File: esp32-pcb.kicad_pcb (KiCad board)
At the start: 2 copper layers, 25.2 x 59.4 mm, 50 parts, among them J1 Conn_01x15_Male, J2 Conn_01x15_Male, Q1 SI2333DDS-T1-GE3, Q2 BSS138Q-7-F, Q3 MMBT3904, Q4 MMBT3904, Q5 BSS138Q-7-F, SW1 RESET, SW2 USER, SW3 SW_DIP_x04, U1 TLV75533, U2 ESP32-WROOM-32, U3 CP2102N-A01-GQFN24

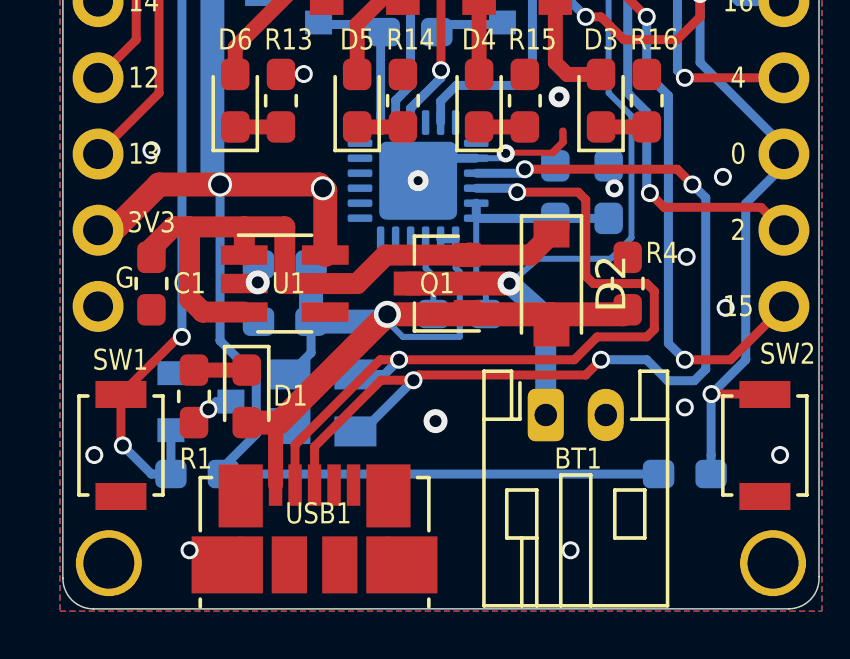
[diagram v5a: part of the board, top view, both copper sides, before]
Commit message: Fix D2 text. Eliminate overlaps
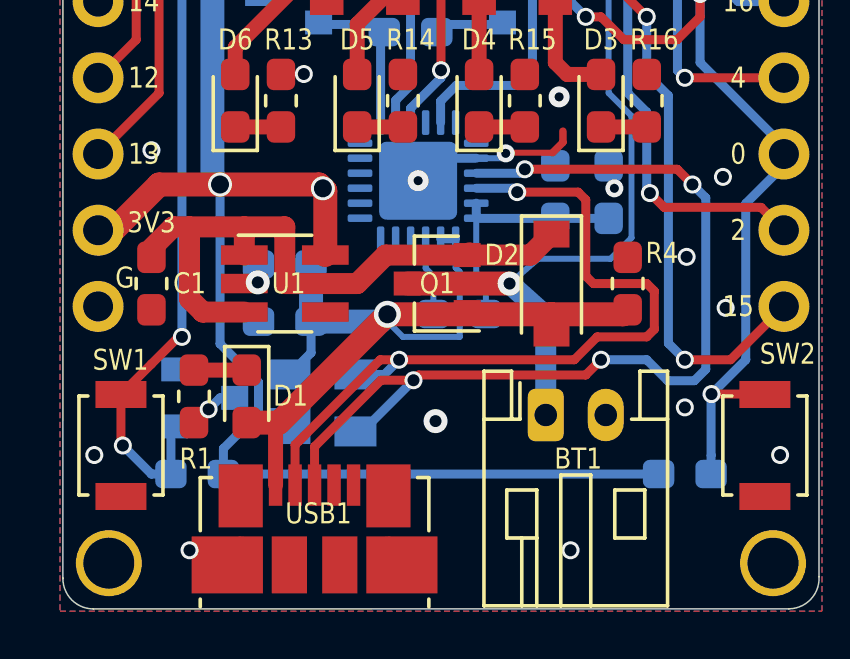
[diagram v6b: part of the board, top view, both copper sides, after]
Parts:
- moved Q5 0.18 mm to (133.9, 120.7)

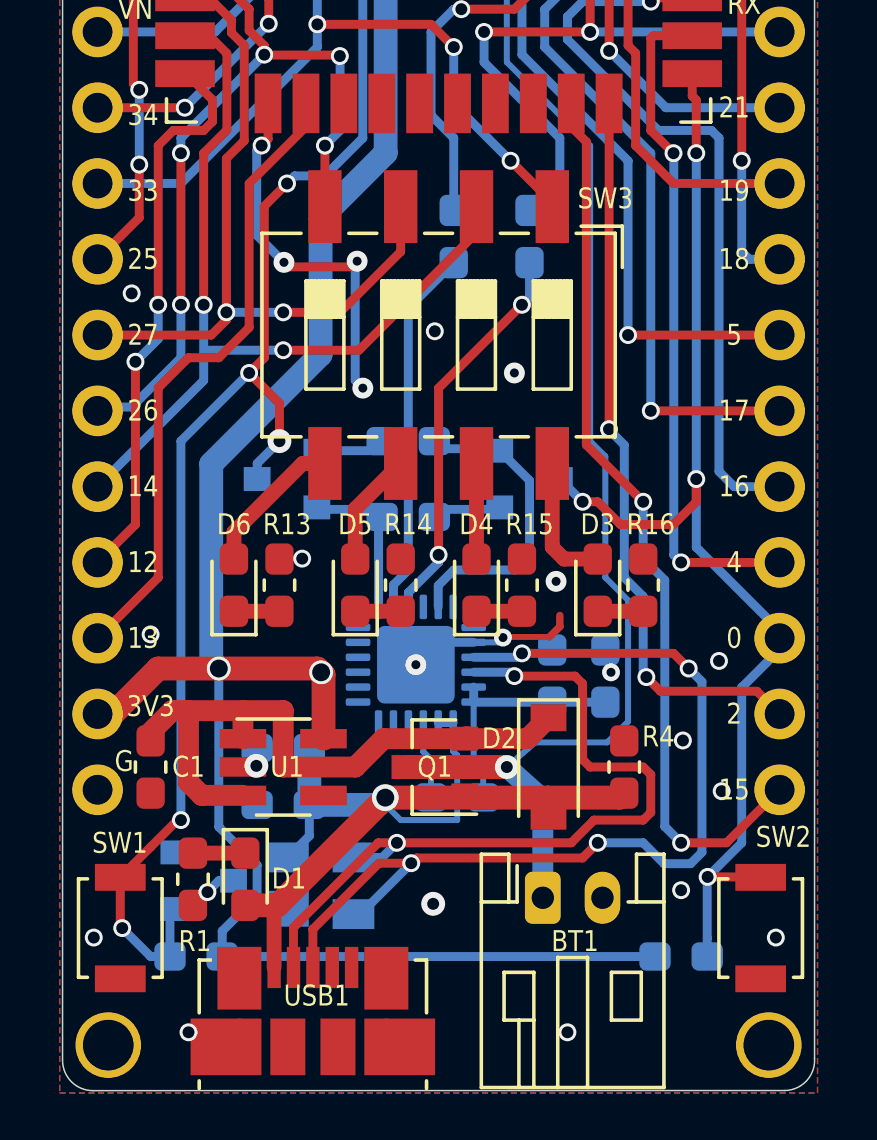
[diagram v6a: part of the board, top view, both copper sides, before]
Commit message: Connect D4 to IO12
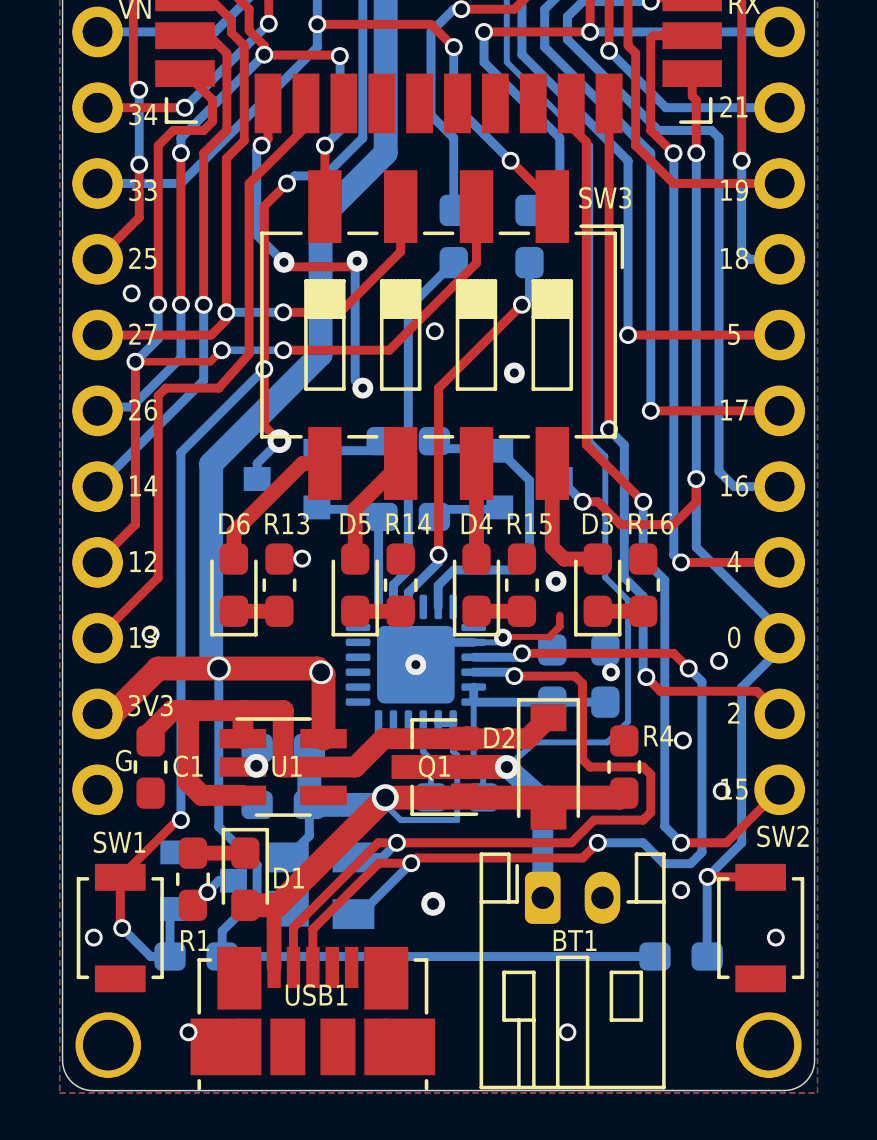
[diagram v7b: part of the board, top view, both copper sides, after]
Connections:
- SW3 pad 2: ESP_IO14 -> ESP_IO12
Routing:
- net ESP_IO12: track 19.0 -> 34.5 mm, vias 2 -> 4
- net ESP_IO14: track 30.2 -> 18.7 mm, vias 2 -> 1

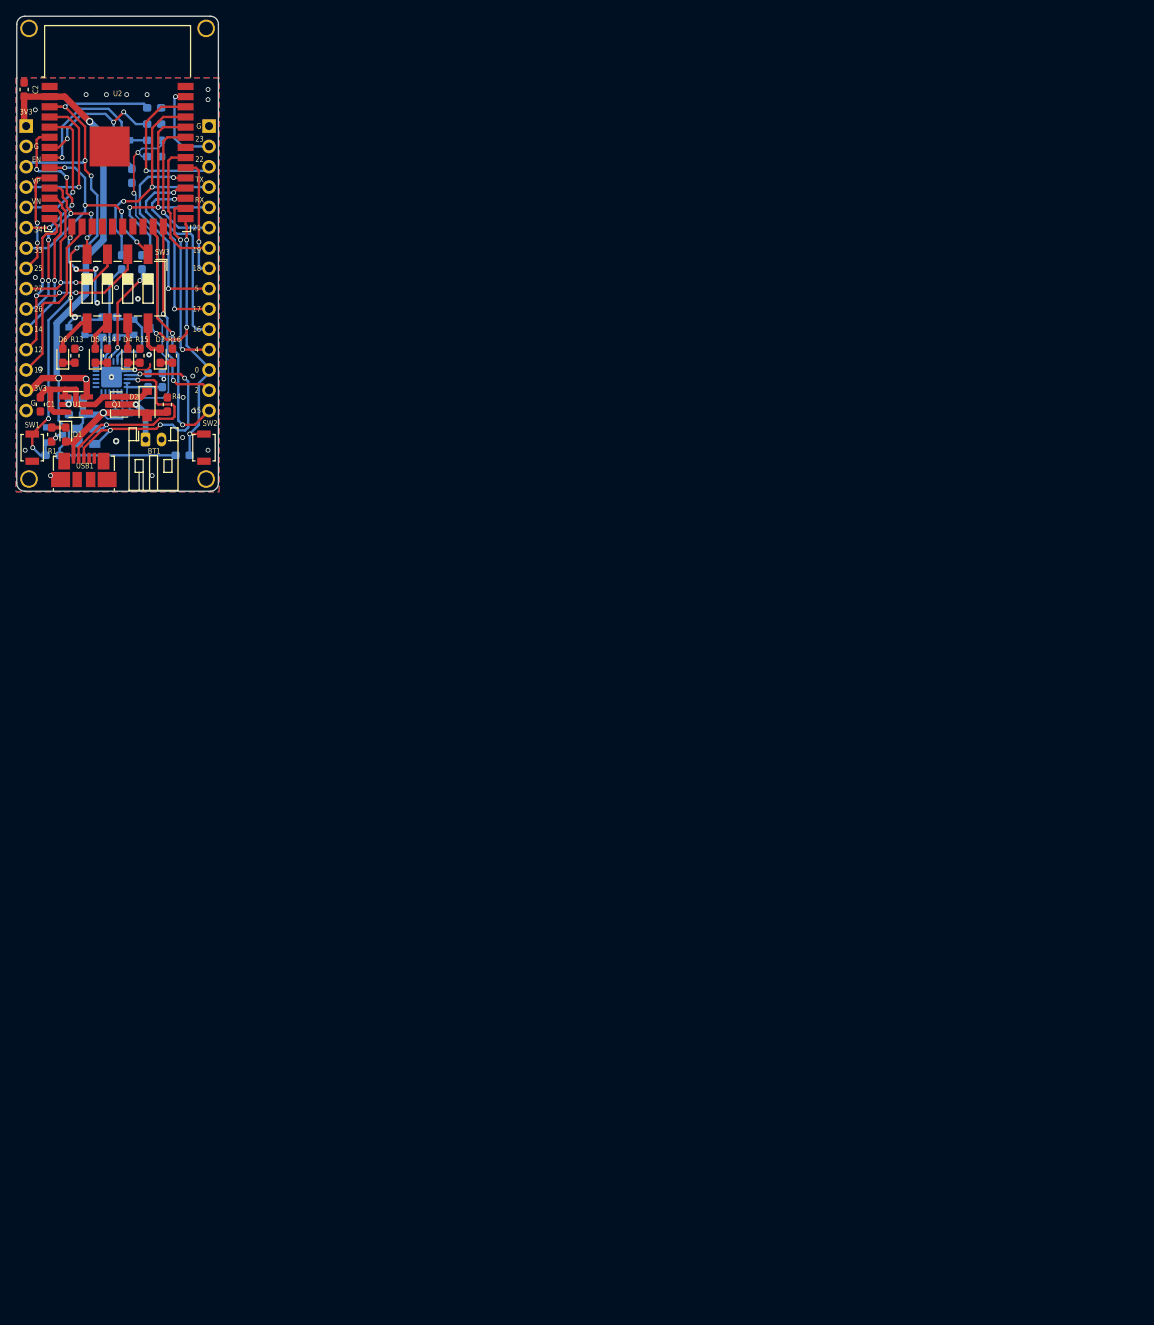
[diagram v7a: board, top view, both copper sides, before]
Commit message: Label diodes with IO ports they are connected to
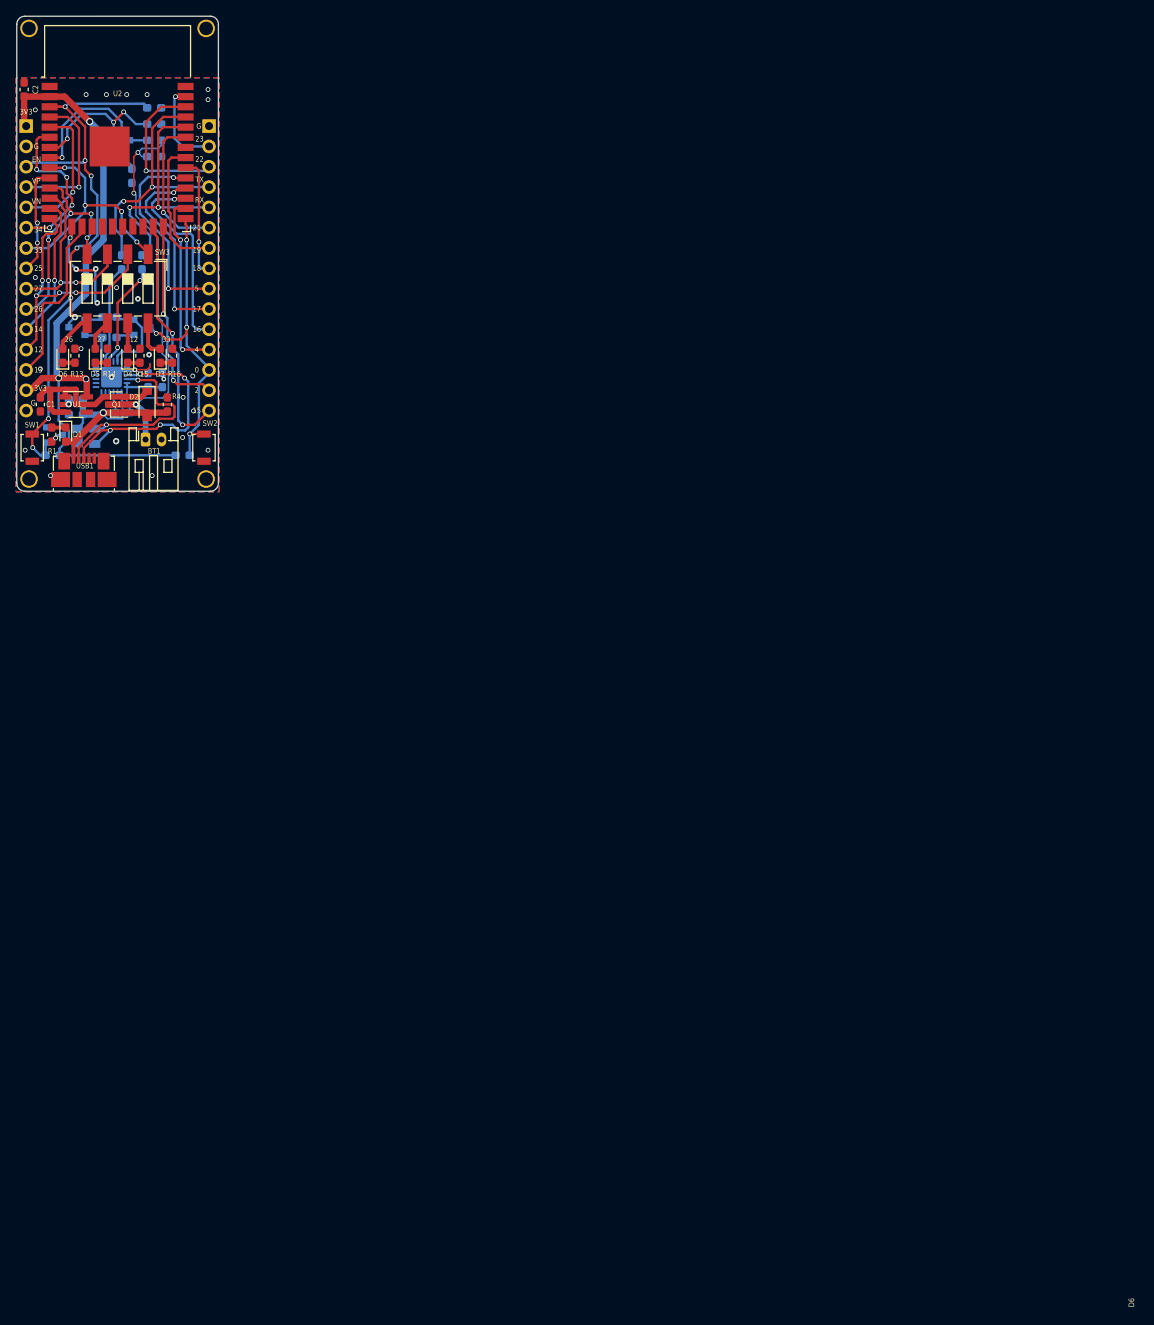
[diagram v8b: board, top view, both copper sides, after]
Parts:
- added ?: , , F.Cu at (134.6, 108.5)
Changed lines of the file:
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@@
   (general
     (thickness 1.6)
-    (drawings 3056)
+    (drawings 3060)
     (tracks 624)
     (zones 0)
-    (modules 50)
+    (modules 51)
     (nets 75)
   )
@@
     (add_net V_BAT_MEASURE)
   )
+  (module "" (layer F.Cu)
+    (at 134.62 108.458)
+    (fp_text reference "" (at 133.858 120.65) (layer F.SilkS)
+      (effects (font (size 1.27 1.27) (thickness 0.15)))
+    )
+    (fp_text value "" (at 133.858 120.65) (layer F.SilkS)
+      (effects (font (size 1.27 1.27) (thickness 0.15)))
+    )
+    (fp_text user D6 (at 133.858 120.65 90) (layer F.SilkS)
+      (effects (font (size 0.7 0.6) (thickness 0.16)))
+    )
+  )
   (module Package_TO_SOT_SMD:SOT-23 (layer B.Cu)
     (at 133.858 120.65)
@@
     (tags "resistor handsolder")
     (attr smd)
-    (fp_text reference R16 (at 2.032 0.254 180) (layer F.SilkS)
-      (effects (font (size 0.7 0.6) (thickness 0.16)))
+    (fp_text reference R16 (at -2.286 0.254 180) (layer F.SilkS)
+      (effects (font (size 0.7 0.6) (thickness 0.15)))
     )
     (fp_text value 470 (at 0 1.43 90) (layer F.Fab)
@@
     (tags "resistor handsolder")
     (attr smd)
-    (fp_text reference R15 (at 2.032 0.254 180) (layer F.SilkS)
-      (effects (font (size 0.7 0.6) (thickness 0.16)))
+    (fp_text reference R15 (at -2.286 0.254 180) (layer F.SilkS)
+      (effects (font (size 0.7 0.6) (thickness 0.15)))
     )
     (fp_text value 470 (at 0 1.43 90) (layer F.Fab)
@@
     (tags "resistor handsolder")
     (attr smd)
-    (fp_text reference R14 (at 2.032 0.254 180) (layer F.SilkS)
-      (effects (font (size 0.7 0.6) (thickness 0.16)))
+    (fp_text reference R14 (at -2.286 0.254 180) (layer F.SilkS)
+      (effects (font (size 0.7 0.6) (thickness 0.15)))
     )
     (fp_text value 470 (at 0 1.43 90) (layer F.Fab)
@@
     (tags "resistor handsolder")
     (attr smd)
-    (fp_text reference R13 (at 2.032 0.254 180) (layer F.SilkS)
-      (effects (font (size 0.7 0.6) (thickness 0.16)))
+    (fp_text reference R13 (at -2.286 0.254 180) (layer F.SilkS)
+      (effects (font (size 0.7 0.6) (thickness 0.15)))
     )
     (fp_text value 470 (at 0 1.43 90) (layer F.Fab)
@@
     (tags "LED handsolder")
     (attr smd)
-    (fp_text reference D6 (at 2.032 0 180) (layer F.SilkS)
+    (fp_text reference D6 (at -2.286 0 180) (layer F.SilkS)
       (effects (font (size 0.7 0.6) (thickness 0.16)))
     )
@@
     (tags "LED handsolder")
     (attr smd)
-    (fp_text reference D5 (at 2.032 0 180) (layer F.SilkS)
-      (effects (font (size 0.7 0.6) (thickness 0.16)))
+    (fp_text reference D5 (at -2.286 0 180) (layer F.SilkS)
+      (effects (font (size 0.7 0.6) (thickness 0.15)))
     )
     (fp_text value LED_BLUE (at 0 1.43 90) (layer F.Fab)
@@
     (tags "LED handsolder")
     (attr smd)
-    (fp_text reference D4 (at 2.032 0 180) (layer F.SilkS)
-      (effects (font (size 0.7 0.6) (thickness 0.16)))
+    (fp_text reference D4 (at -2.286 0 180) (layer F.SilkS)
+      (effects (font (size 0.7 0.6) (thickness 0.15)))
     )
     (fp_text value LED_GREEN (at 0 1.43 90) (layer F.Fab)
@@
     (tags "LED handsolder")
     (attr smd)
-    (fp_text reference D3 (at 2.032 0 180) (layer F.SilkS)
-      (effects (font (size 0.7 0.6) (thickness 0.16)))
+    (fp_text reference D3 (at -2.286 0 180) (layer F.SilkS)
+      (effects (font (size 0.7 0.6) (thickness 0.15)))
     )
     (fp_text value LED_RED (at 0 1.43 90) (layer F.Fab)
@@
     )
   )
+  (gr_text 33 (at 147.828 108.712) (layer F.SilkS)
+    (effects (font (size 0.7 0.6) (thickness 0.15)))
+  )
+  (gr_text 12 (at 143.764 108.712) (layer F.SilkS)
+    (effects (font (size 0.7 0.6) (thickness 0.15)))
+  )
+  (gr_text 27 (at 139.7 108.712) (layer F.SilkS)
+    (effects (font (size 0.7 0.6) (thickness 0.15)))
+  )
+  (gr_text 26 (at 135.636 108.712) (layer F.SilkS)
+    (effects (font (size 0.7 0.6) (thickness 0.15)))
+  )
   (gr_text "To the moon!" (at 137.414 95.123) (layer B.SilkS)
